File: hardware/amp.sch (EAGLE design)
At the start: 1 part

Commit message: amp update
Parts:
- added U$1: STK465HORIZ-BOTTOM, Simplex-ICs:STK465HORIZ-BOTTOM
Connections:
- new net GND: U$1G$1.3
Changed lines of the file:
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@@
 <part name="FRAME1" library="frames" deviceset="DOCFIELD" device="" value="ihaaa"/>
 <part name="U$7" library="SparkFun" deviceset="OSHW-LOGO" device="M"/>
+<part name="U$1" library="Simplex-ICs" deviceset="STK465" device="HORIZ-BOTTOM"/>
+<part name="GND1" library="supply1" deviceset="GND" device=""/>
 </parts>
 <sheets>
@@
 <instance part="FRAME1" gate="G$1" x="373.38" y="17.78"/>
 <instance part="U$7" gate="G$1" x="454.66" y="45.72"/>
+<instance part="U$1" gate="G$1" x="185.42" y="238.76"/>
+<instance part="U$1" gate="G$2" x="238.76" y="238.76"/>
+<instance part="GND1" gate="1" x="170.18" y="223.52"/>
 </instances>
 <busses>
 </busses>
 <nets>
+<net name="GND" class="0">
+<segment>
+<pinref part="U$1" gate="G$1" pin="3"/>
+<wire x1="175.26" y1="233.68" x2="170.18" y2="233.68" width="0.1524" layer="91"/>
+<wire x1="170.18" y1="233.68" x2="170.18" y2="226.06" width="0.1524" layer="91"/>
+<pinref part="GND1" gate="1" pin="GND"/>
+</segment>
+</net>
 </nets>
 </sheet>

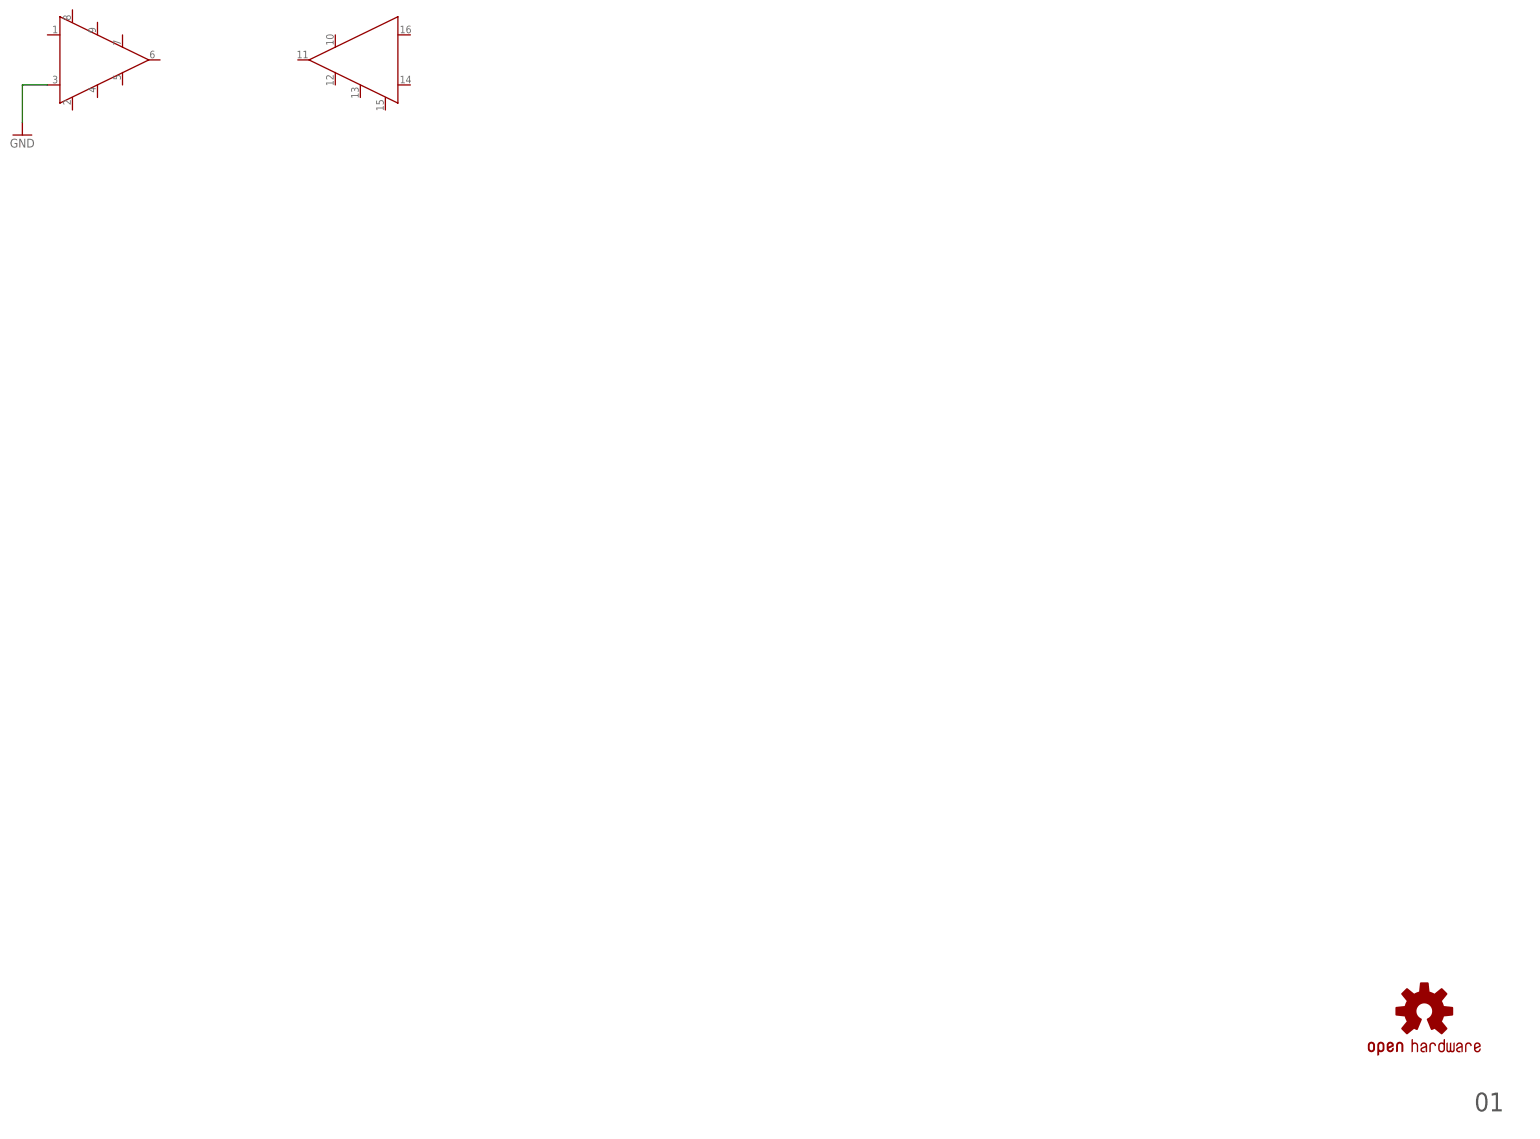
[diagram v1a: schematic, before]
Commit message: amplifier schematic
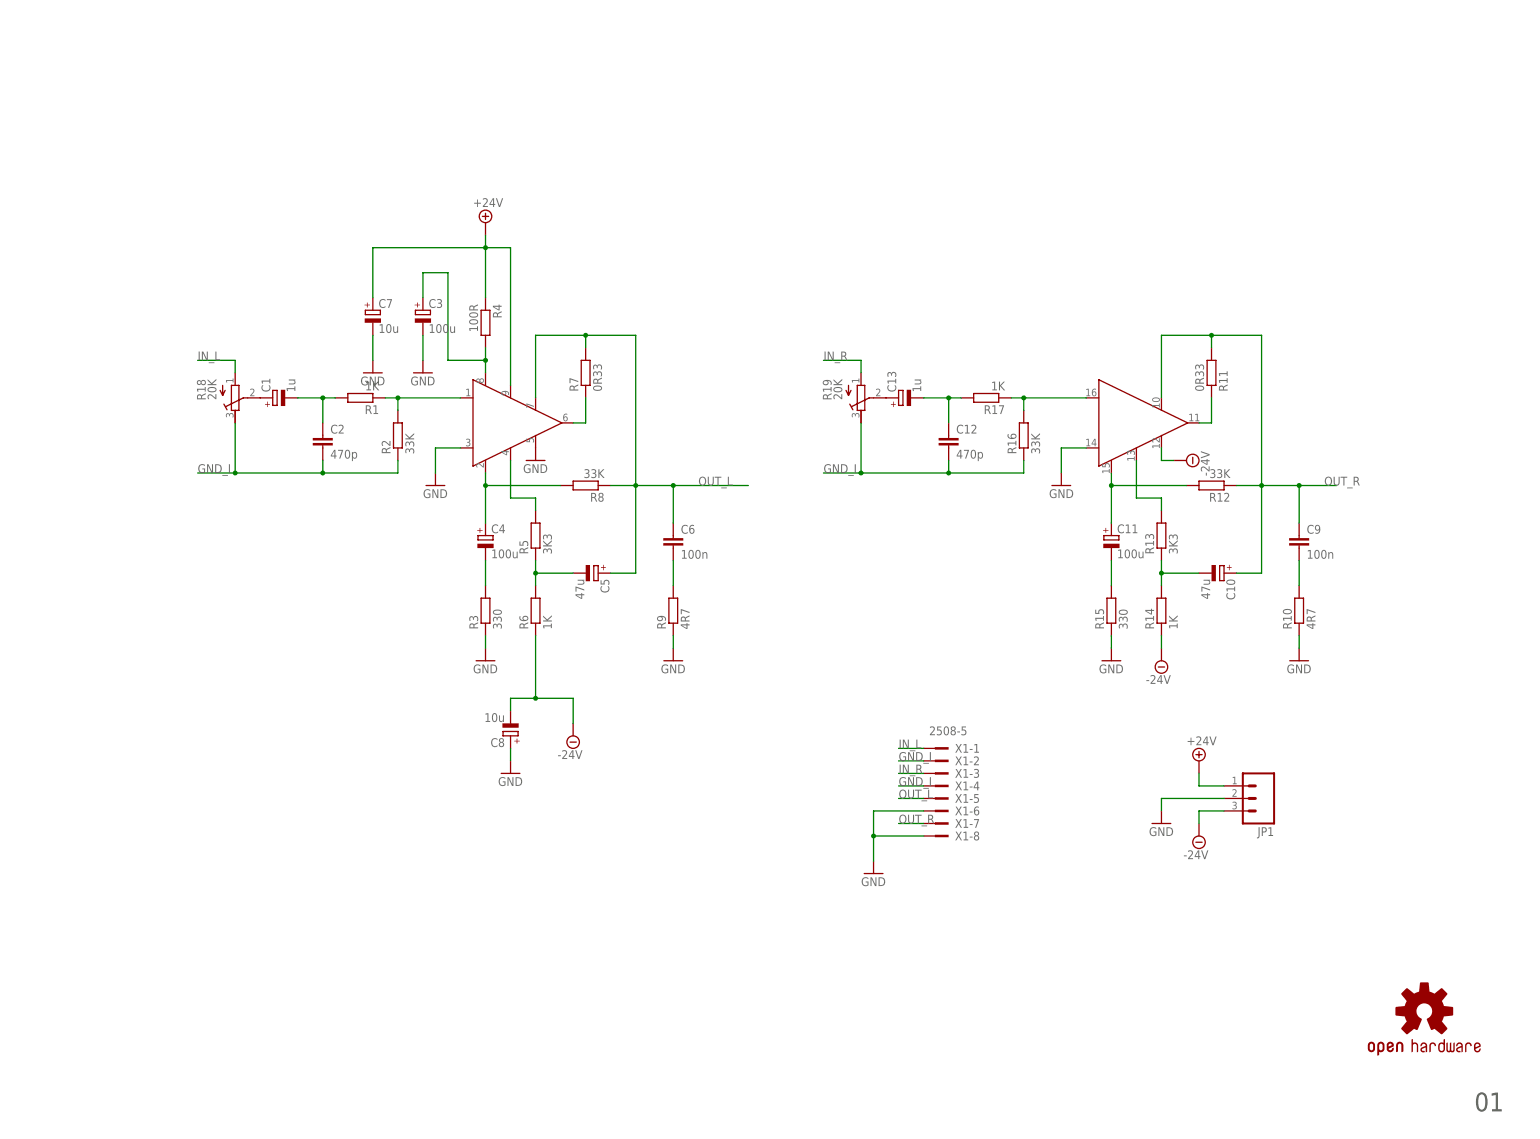
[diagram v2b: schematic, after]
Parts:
- added C1, C13: 1u, rcl:CPOL-EUB
- added C10, C5: 47u, rcl:CPOL-EUF
- added C11, C3, C4: 100u, rcl:CPOL-EUG
- added C12, C2: 470p, rcl:C-EUC0805
- added C6, C9: 100n, rcl:C-EUC0805K
- added C7, C8: 10u, rcl:CPOL-EUF
- added JP1: (no value), SparkFun-Connectors:M03JST-PTH
- added R1, R17: 1K, rcl:R-EU_R0805W
- added R10, R9: 4R7, rcl:R-EU_0617/17
- added R11, R7: 0R33, rcl:R-EU_0922/22
- added R12, R8: 33K, rcl:R-EU_0617/17
- added R13, R5: 3K3, rcl:R-EU_0617/17
- added R14, R6: 1K, rcl:R-EU_0617/17
- added R15, R3: 330, rcl:R-EU_0617/17
- added R16, R2: 33K, rcl:R-EU_R0805W
- added R18, R19: 20K, rcl:R-TRIMM3339P
- added R4: 100R, rcl:R-EU_0617/17
- added X1: 2508-5, Simplex-Connectors:2508-5
- U$1: value STK465HORIZ-BOTTOM -> STK465
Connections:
- new net +24V: C7.+, JP1.1, R4.1, U$1G$1.9
- new net -24V: C8.-, JP1.3, R14.1, R6.1, U$1G$2.12
- new net GND_I: C12.2, C2.2, R16.1, R18.E, R19.E, R2.1, X1-2.KL, X1-4.KL
- new net IN_L: R18.A, X1-1.KL
- new net IN_R: R19.A, X1-3.KL
- new net N$1: C4.-, R3.2
- new net N$10: C1.+, R18.S
- new net N$11: C13.+, R19.S
- new net N$12: R11.1, U$1G$2.11
- new net N$13: C11.-, R15.2
- new net N$14: R16.2, R17.1, U$1G$2.16
- new net N$15: C12.1, C13.-, R17.2
- new net N$17: C11.+, R12.2, U$1G$2.15
- new net N$18: C10.-, R13.1, R14.2
- new net N$19: R13.2, U$1G$2.13
- new net N$2: C4.+, R8.2, U$1G$1.2
- new net N$20: C9.2, R10.2
- new net N$3: C5.-, R5.1, R6.2
- new net N$4: C6.2, R9.2
- new net N$5: R7.1, U$1G$1.6
- new net N$6: C3.+, R4.2, U$1G$1.8
- new net N$7: R5.2, U$1G$1.4
- new net N$8: R1.1, R2.2, U$1G$1.1
- new net N$9: C1.-, C2.1, R1.2
- new net OUT_L: C5.+, C6.1, R7.2, R8.1, U$1G$1.7, X1-5.KL
- new net OUT_R: C10.+, C9.1, R11.2, R12.1, U$1G$2.10, X1-7.KL
- net GND: now also C3.-, C7.-, C8.+, JP1.2, R10.1, R15.1, R3.1, R9.1, U$1G$1.5, U$1G$2.14, X1-6.KL, X1-8.KL

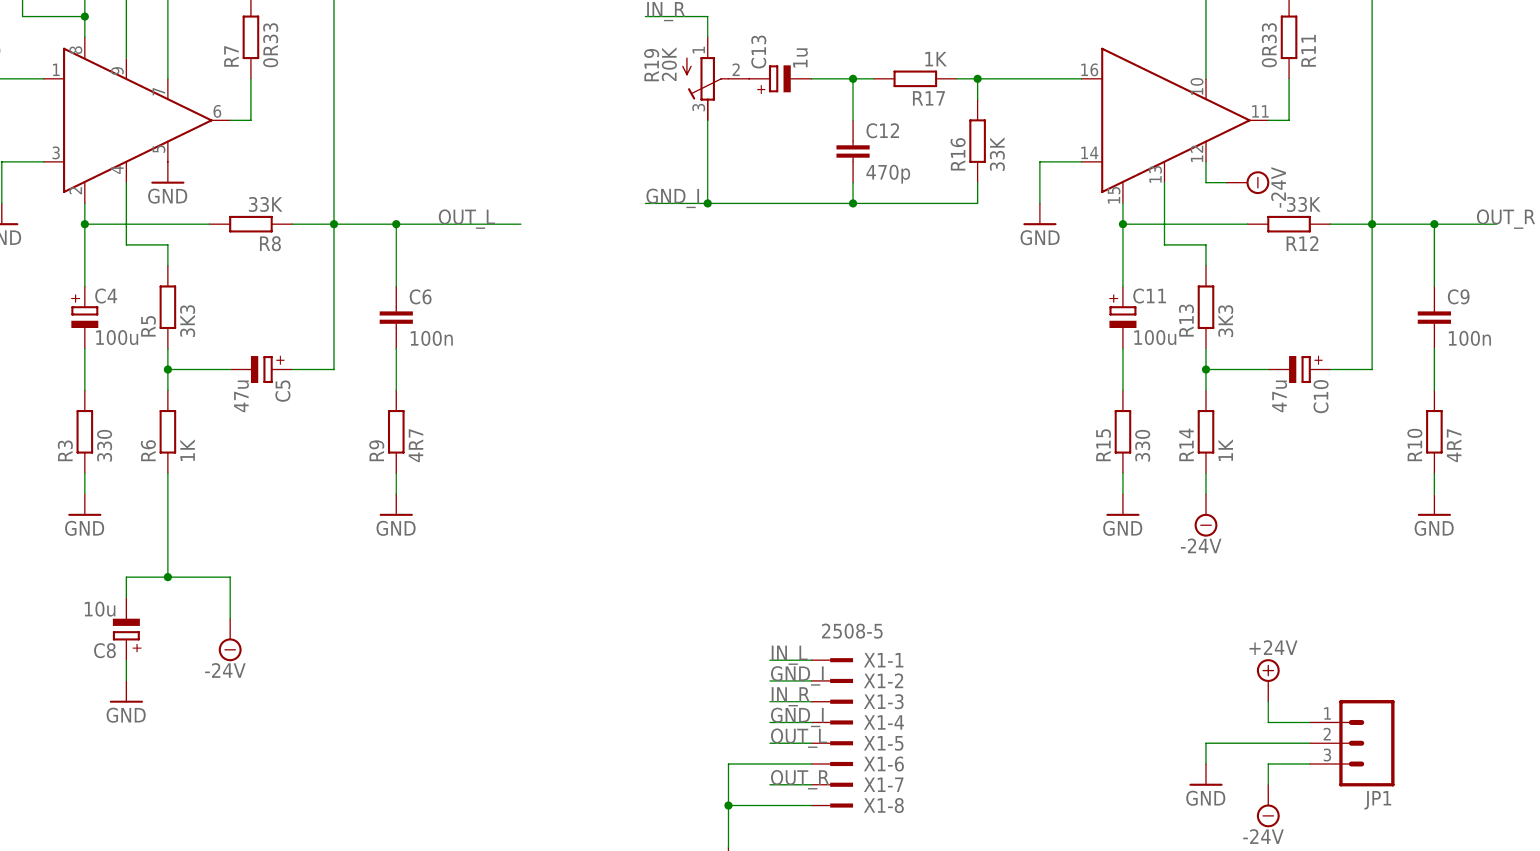
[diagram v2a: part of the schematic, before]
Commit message: amp routed
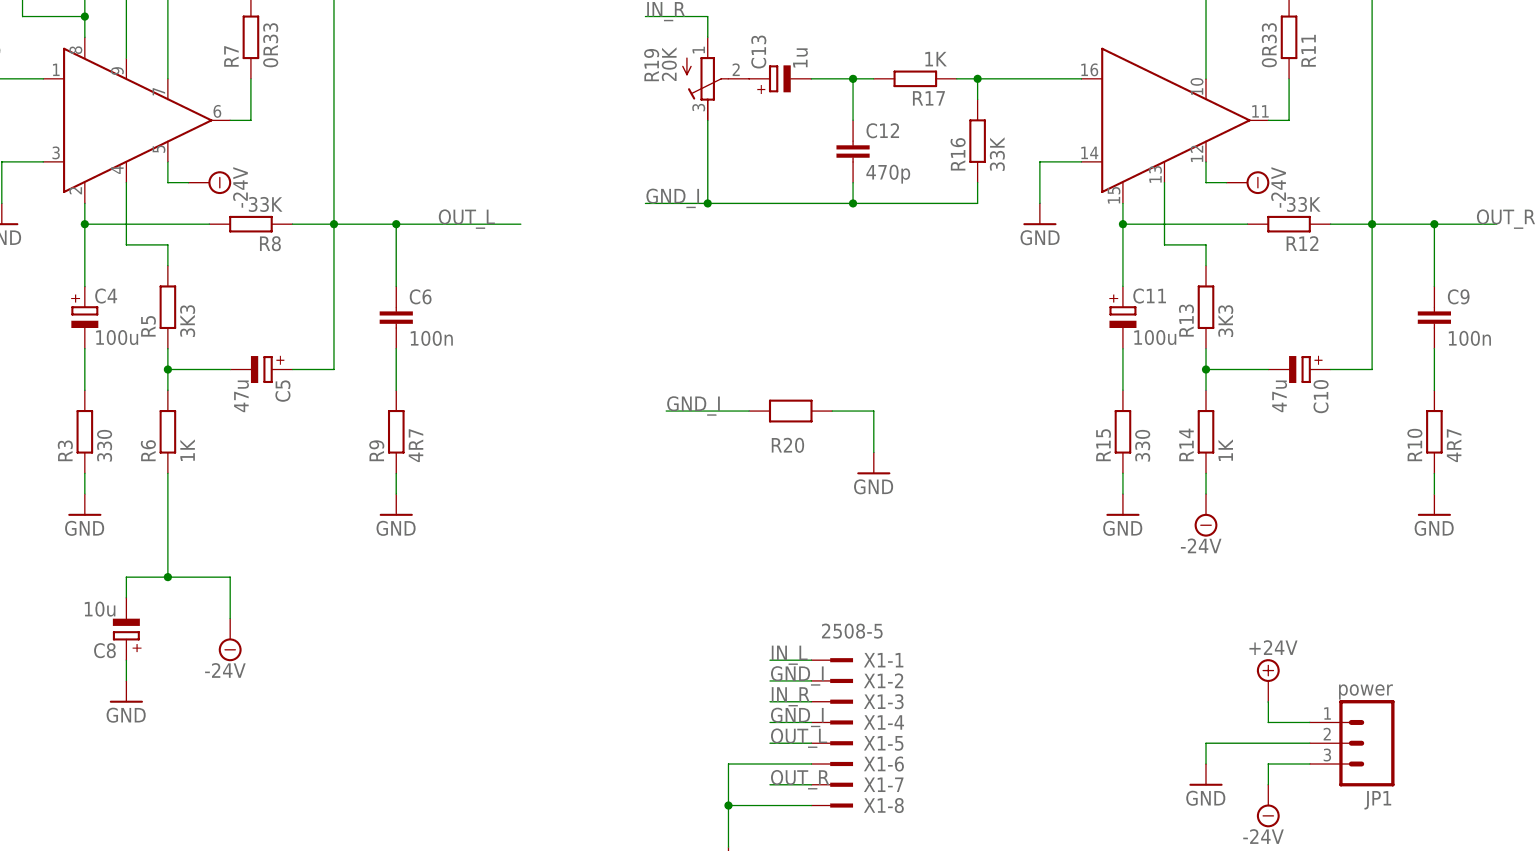
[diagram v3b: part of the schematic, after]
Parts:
- added R20: 0R_0805, Simplex-Jumpers:0R_0805
- C6, C9: device rcl:C-EUC0805K -> capacitor-wima:C10/5
- JP1: value (none) -> power; device SparkFun-Connectors:M03JST-PTH -> SparkFun-Connectors:M03PTH
- U$1: value STK465 -> STK465HORIZ-BOTTOM
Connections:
- net -24V: now also U$1G$1.5
- net GND: now also R20.P$2; no longer U$1G$1.5
- net GND_I: now also R20.P$1

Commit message: sent to manufacture
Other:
- moved on the sheet: C1, C10, C11, C12, C13, C2, C3, C4, C5, C6, C7, C8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
